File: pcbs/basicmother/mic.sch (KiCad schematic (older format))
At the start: 15 parts, among them P10 mic_conn, U7 TL082

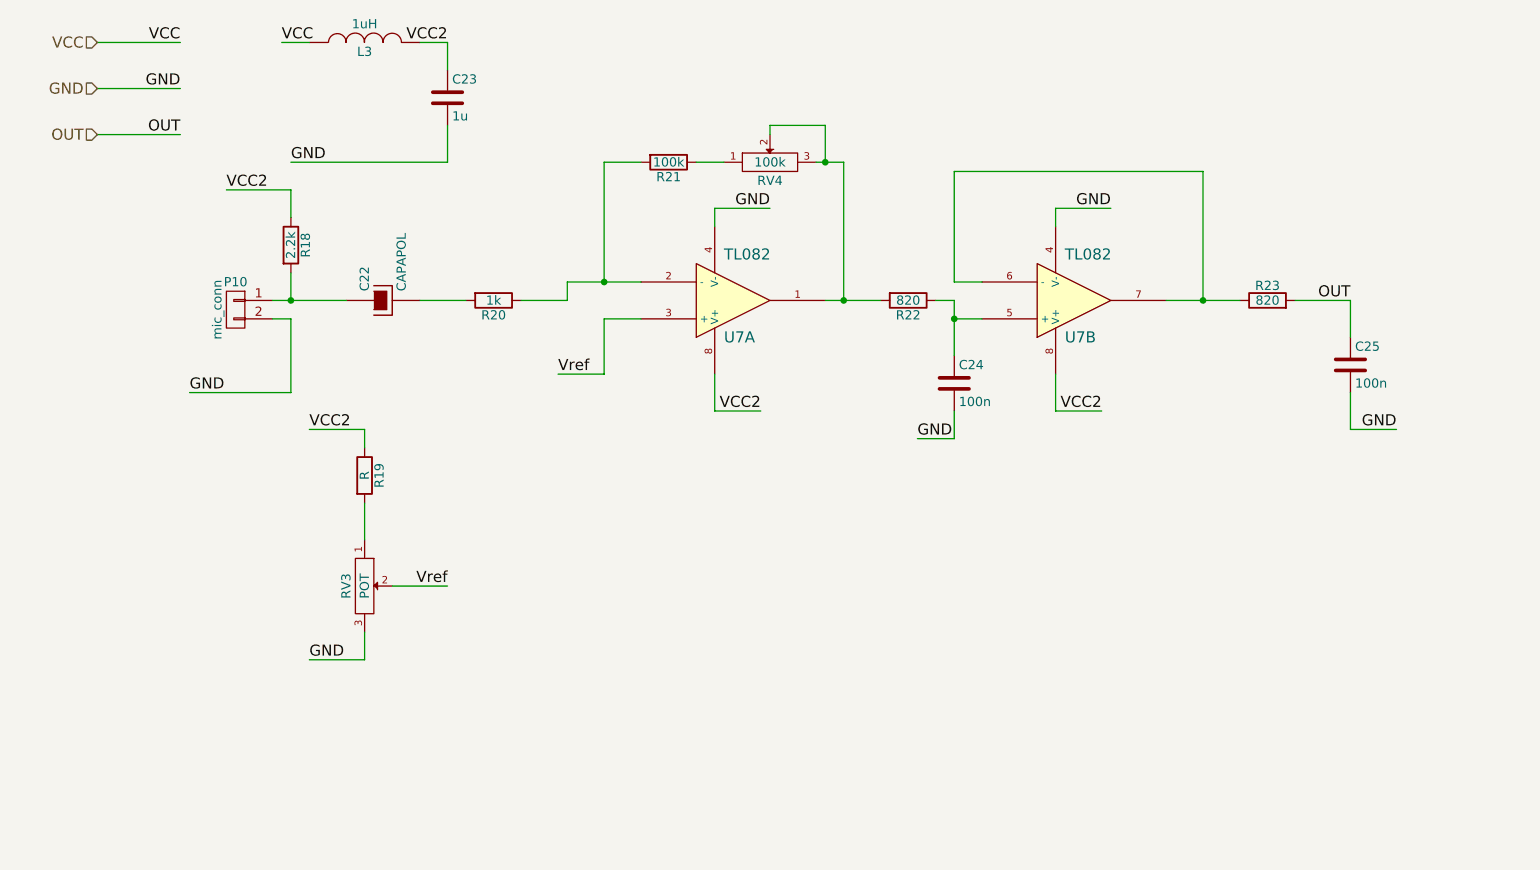
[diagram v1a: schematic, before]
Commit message: Actualizo el esquematico de la placa principal
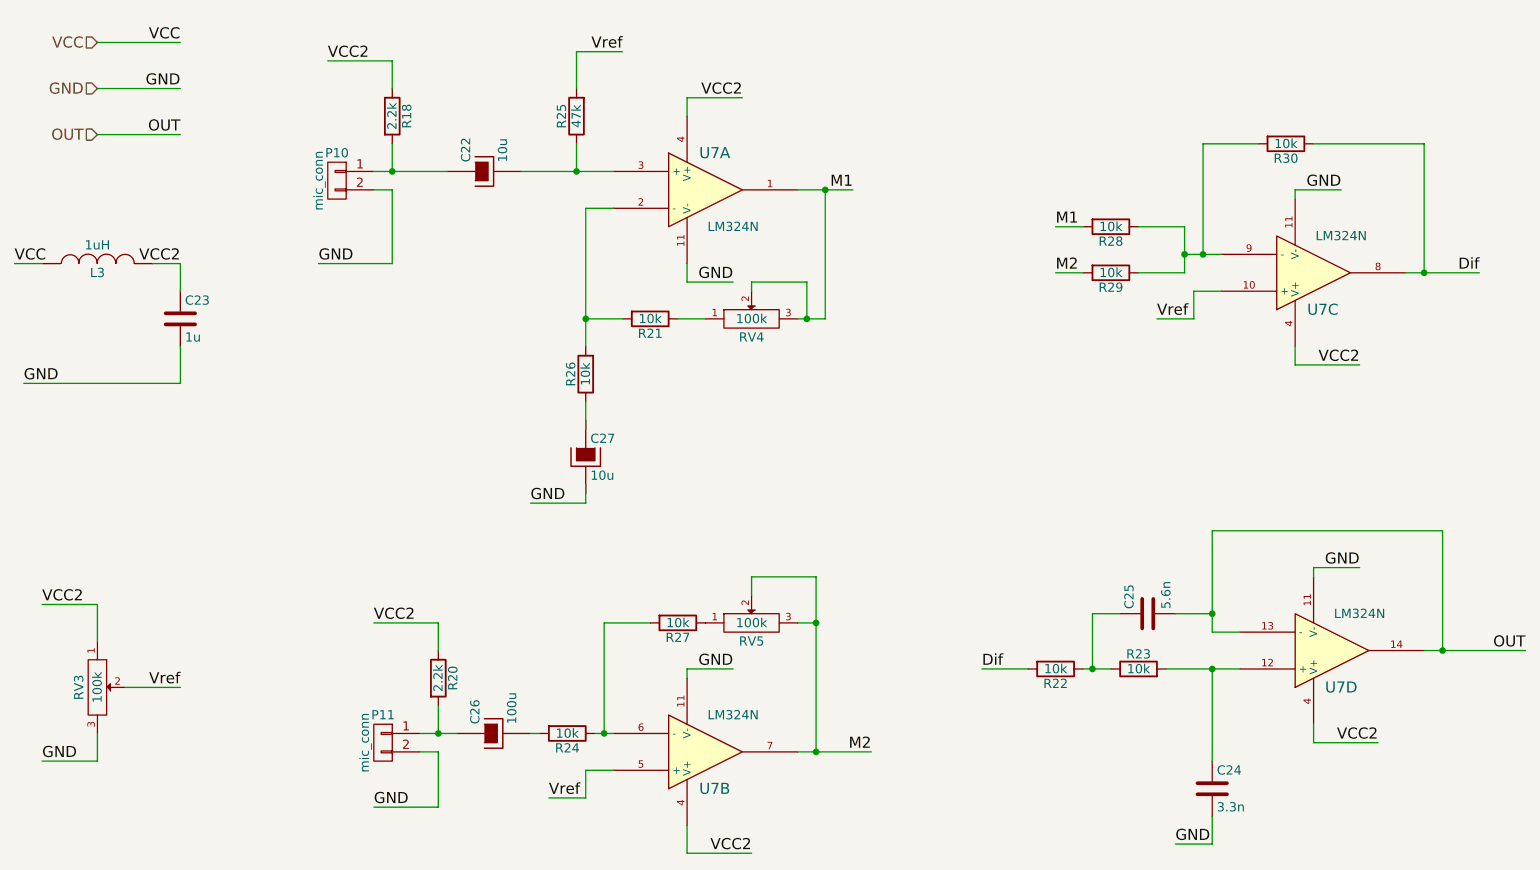
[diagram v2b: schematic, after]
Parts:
- removed R19: R, symbol R
- removed U7: TL082, symbol TL082
- added C26: 100u, symbol CAPAPOL
- added C27: 10u, symbol CP
- added P11: mic_conn, symbol CONN_01X02
- added R24, R26, R27, R28, R29, R30: 10k, symbol R
- added R25: 47k, symbol R
- added RV5: 100k, symbol POT
- added U7: LM324N, symbol LM324N
- C22: value CAPAPOL -> 10u
- C24: value 100n -> 3.3n
- C25: value 100n -> 5.6n
- R20: value 1k -> 2.2k
- R21: value 100k -> 10k
- R22, R23: value 820 -> 10k
- RV3: value POT -> 100k
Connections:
- net GND: now also P11.2 (P2), U7.11 (V-), U7.11 (V-), U7.11 (V-), U7.11 (V-); no longer C25.2
- net OUT: now also C25.2, U7.13 (-), U7.14; no longer C25.1, R23.2
- net VCC2: now also R20.1, RV3.1, U7.4 (V+), U7.4 (V+), U7.4 (V+), U7.4 (V+)
- net Vref: now also R25.2, U7.10 (+), U7.5 (+)
- net at C22.2: now also R25.1, U7.3 (+); no longer R20.2
- net M1: now reaches RV4.2, RV4.3
- net M1: now also R28.2, U7.1; no longer R22.2
- net at R21.2: now also R26.2, U7.2 (-); no longer R20.1
- net at R22.1: now also C25.1, R23.1; no longer C24.1
- new net: C24.1, R23.2, U7.12 (+)
- new net: C26.1, P11.1 (P1), R20.2
- new net: C26.2, R24.2
- new net: R28.1, R29.1, R30.2, U7.9 (-)
- new net: R24.1, R27.2, U7.6 (-)
- new net: R27.1, RV5.1
- new net Dif: R22.2, R30.1, U7.8
- new net M2: R29.2, RV5.2, RV5.3, U7.7
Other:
- moved on the sheet: C22, C23, C24, C25, L3, P10, R18, R21, R22, R23, RV3, RV4

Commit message: saque el micro para el control de los ojitos y lo pase a una placa aparte, ademas agregue un doble microfono
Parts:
- removed R30: 10k, symbol R
- added RV6: 100k, Socket_Strips:Socket_Strip_Straight_1x03, symbol POT
- C18: renamed from C23; footprint (none) -> Capacitors_ThroughHole:C_Disc_D3_P2.5
- C19: renamed from C22; footprint (none) -> Capacitors_ThroughHole:C_Disc_D3_P2.5
- C20: renamed from C26; footprint (none) -> Capacitors_ThroughHole:C_Radial_D5_L6_P2.5
- C21: renamed from C27; footprint (none) -> Capacitors_ThroughHole:C_Radial_D5_L6_P2.5
- C22: renamed from C25; footprint (none) -> Capacitors_ThroughHole:C_Disc_D3_P2.5
- C23: renamed from C24; footprint (none) -> Capacitors_ThroughHole:C_Disc_D3_P2.5
- L3, R18: footprint (none) -> Resistors_ThroughHole:Resistor_Horizontal_RM10mm
- P10: renamed from P11; footprint (none) -> Socket_Strips:Socket_Strip_Straight_1x02
- P9: renamed from P10; footprint (none) -> Socket_Strips:Socket_Strip_Straight_1x02
- R19: renamed from R20; footprint (none) -> Resistors_ThroughHole:Resistor_Horizontal_RM10mm
- R20: renamed from R24; footprint (none) -> Resistors_ThroughHole:Resistor_Horizontal_RM10mm
- R21: renamed from R25; footprint (none) -> Resistors_ThroughHole:Resistor_Horizontal_RM10mm
- R22: renamed from R26; footprint (none) -> Resistors_ThroughHole:Resistor_Horizontal_RM10mm
- R23: renamed from R21; footprint (none) -> Resistors_ThroughHole:Resistor_Horizontal_RM10mm
- R24: renamed from R27; footprint (none) -> Resistors_ThroughHole:Resistor_Horizontal_RM10mm
- R25: renamed from R22; footprint (none) -> Resistors_ThroughHole:Resistor_Horizontal_RM10mm
- R26: renamed from R28; footprint (none) -> Resistors_ThroughHole:Resistor_Horizontal_RM10mm
- R27: renamed from R29; footprint (none) -> Resistors_ThroughHole:Resistor_Horizontal_RM10mm
- R28: renamed from R23; footprint (none) -> Resistors_ThroughHole:Resistor_Horizontal_RM10mm
- RV3, RV4, RV5: footprint (none) -> Socket_Strips:Socket_Strip_Straight_1x03
- U8: renamed from U7; footprint (none) -> Sockets_DIP:DIP-14__300_ELL
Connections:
- net Dif: now also RV6.2, RV6.3
- net at R26.1, R27.1, U8.9 (-): now also RV6.1
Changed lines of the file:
@@
 $EndDescr
 $Comp
-L CONN_01X02 P10
+L CONN_01X02 P9
 U 1 1 55280813
 P 2600 1950
-F 0 "P10" H 2600 2100 50  0000 C CNN
+F 0 "P9" H 2600 2100 50  0000 C CNN
 F 1 "mic_conn" V 2700 1950 50  0000 C CNN
-F 2 "" H 2600 1950 60  0000 C CNN
+F 2 "Socket_Strips:Socket_Strip_Straight_1x02" H 2600 1950 60  0001 C CNN
 F 3 "" H 2600 1950 60  0000 C CNN
 	1    2600 1950
@@
 F 0 "R18" V 2980 1600 50  0000 C CNN
 F 1 "2.2k" V 2900 1600 50  0000 C CNN
-F 2 "" V 2830 1600 30  0000 C CNN
+F 2 "Resistors_ThroughHole:Resistor_Horizontal_RM10mm" V 2830 1600 30  0001 C CNN
 F 3 "" H 2900 1600 30  0000 C CNN
 	1    2900 1600
@@
 Connection ~ 2900 1900
 $Comp
-L CAPAPOL C22
+L CAPAPOL C19
 U 1 1 552809F6
 P 3400 1900
-F 0 "C22" H 3450 2000 50  0000 L CNN
+F 0 "C19" H 3450 2000 50  0000 L CNN
 F 1 "10u" H 3450 1800 50  0000 L CNN
-F 2 "" H 3500 1750 30  0000 C CNN
+F 2 "Capacitors_ThroughHole:C_Disc_D3_P2.5" H 3500 1750 30  0001 C CNN
 F 3 "" H 3400 1900 300 0000 C CNN
 	1    3400 1900
@@
 $EndComp
 $Comp
-L R R21
+L R R23
 U 1 1 55280CA5
 P 4300 2700
-F 0 "R21" V 4380 2700 50  0000 C CNN
+F 0 "R23" V 4380 2700 50  0000 C CNN
 F 1 "10k" V 4300 2700 50  0000 C CNN
-F 2 "" V 4230 2700 30  0000 C CNN
+F 2 "Resistors_ThroughHole:Resistor_Horizontal_RM10mm" V 4230 2700 30  0001 C CNN
 F 3 "" H 4300 2700 30  0000 C CNN
 	1    4300 2700
@@
 	4150 2700 3950 2700
 $Comp
-L R R22
+L R R25
 U 1 1 55280E9E
 P 6500 4600
-F 0 "R22" V 6580 4600 50  0000 C CNN
+F 0 "R25" V 6580 4600 50  0000 C CNN
 F 1 "10k" V 6500 4600 50  0000 C CNN
-F 2 "" V 6430 4600 30  0000 C CNN
+F 2 "Resistors_ThroughHole:Resistor_Horizontal_RM10mm" V 6430 4600 30  0001 C CNN
 F 3 "" H 6500 4600 30  0000 C CNN
 	1    6500 4600
@@
 F 0 "RV3" H 1300 4600 50  0000 C CNN
 F 1 "100k" H 1300 4700 50  0000 C CNN
-F 2 "" H 1300 4700 60  0000 C CNN
+F 2 "Socket_Strips:Socket_Strip_Straight_1x03" H 1300 4700 60  0001 C CNN
 F 3 "" H 1300 4700 60  0000 C CNN
 	1    1300 4700
@@
 Vref
 $Comp
-L R R23
+L R R28
 U 1 1 552815BA
 P 6950 4600
-F 0 "R23" V 7030 4600 50  0000 C CNN
+F 0 "R28" V 7030 4600 50  0000 C CNN
 F 1 "10k" V 6950 4600 50  0000 C CNN
-F 2 "" V 6880 4600 30  0000 C CNN
+F 2 "Resistors_ThroughHole:Resistor_Horizontal_RM10mm" V 6880 4600 30  0001 C CNN
 F 3 "" H 6950 4600 30  0000 C CNN
 	1    6950 4600
@@
 $EndComp
 $Comp
-L C C25
+L C C22
 U 1 1 55281618
 P 7000 4300
-F 0 "C25" H 7025 4400 50  0000 L CNN
+F 0 "C22" H 7025 4400 50  0000 L CNN
 F 1 "5.6n" H 7025 4200 50  0000 L CNN
-F 2 "" H 7038 4150 30  0000 C CNN
+F 2 "Capacitors_ThroughHole:C_Disc_D3_P2.5" H 7038 4150 30  0001 C CNN
 F 3 "" H 7000 4300 60  0000 C CNN
 	1    7000 4300
@@
 $EndComp
 $Comp
-L C C24
+L C C23
 U 1 1 55287955
 P 7350 5250
-F 0 "C24" H 7375 5350 50  0000 L CNN
+F 0 "C23" H 7375 5350 50  0000 L CNN
 F 1 "3.3n" H 7375 5150 50  0000 L CNN
-F 2 "" H 7388 5100 30  0000 C CNN
+F 2 "Capacitors_ThroughHole:C_Disc_D3_P2.5" H 7388 5100 30  0001 C CNN
 F 3 "" H 7350 5250 60  0000 C CNN
 	1    7350 5250
@@
 F 0 "RV4" H 4850 2600 50  0000 C CNN
 F 1 "100k" H 4850 2700 50  0000 C CNN
-F 2 "" H 4850 2700 60  0000 C CNN
+F 2 "Socket_Strips:Socket_Strip_Straight_1x03" H 4850 2700 60  0001 C CNN
 F 3 "" H 4850 2700 60  0000 C CNN
 	1    4850 2700
@@
 F 0 "L3" V 1250 2400 50  0000 C CNN
 F 1 "1uH" V 1400 2400 50  0000 C CNN
-F 2 "" H 1300 2400 60  0000 C CNN
+F 2 "Resistors_ThroughHole:Resistor_Horizontal_RM10mm" H 1300 2400 60  0001 C CNN
 F 3 "" H 1300 2400 60  0000 C CNN
 	1    1300 2400
@@
 $EndComp
 $Comp
-L C C23
+L C C18
 U 1 1 55288DAC
 P 1750 2700
-F 0 "C23" H 1775 2800 50  0000 L CNN
+F 0 "C18" H 1775 2800 50  0000 L CNN
 F 1 "1u" H 1775 2600 50  0000 L CNN
-F 2 "" H 1788 2550 30  0000 C CNN
+F 2 "Capacitors_ThroughHole:C_Disc_D3_P2.5" H 1788 2550 30  0001 C CNN
 F 3 "" H 1750 2700 60  0000 C CNN
 	1    1750 2700
@@
 OUT
 $Comp
-L CONN_01X02 P11
+L CONN_01X02 P10
 U 1 1 5531C027
 P 2850 5000
-F 0 "P11" H 2850 5150 50  0000 C CNN
+F 0 "P10" H 2850 5150 50  0000 C CNN
 F 1 "mic_conn" V 2950 5000 50  0000 C CNN
-F 2 "" H 2850 5000 60  0000 C CNN
+F 2 "Socket_Strips:Socket_Strip_Straight_1x02" H 2850 5000 60  0001 C CNN
 F 3 "" H 2850 5000 60  0000 C CNN
 	1    2850 5000
@@
 $EndComp
 $Comp
-L R R20
+L R R19
 U 1 1 5531C02D
 P 3150 4650
-F 0 "R20" V 3230 4650 50  0000 C CNN
+F 0 "R19" V 3230 4650 50  0000 C CNN
 F 1 "2.2k" V 3150 4650 50  0000 C CNN
-F 2 "" V 3080 4650 30  0000 C CNN
+F 2 "Resistors_ThroughHole:Resistor_Horizontal_RM10mm" V 3080 4650 30  0001 C CNN
 F 3 "" H 3150 4650 30  0000 C CNN
 	1    3150 4650
@@
 Connection ~ 3150 4950
 $Comp
-L CAPAPOL C26
+L CAPAPOL C20
 U 1 1 5531C03D
 P 3450 4950
-F 0 "C26" H 3500 5050 50  0000 L CNN
+F 0 "C20" H 3500 5050 50  0000 L CNN
 F 1 "100u" H 3500 4850 50  0000 L CNN
-F 2 "" H 3550 4800 30  0000 C CNN
+F 2 "Capacitors_ThroughHole:C_Radial_D5_L6_P2.5" H 3550 4800 30  0001 C CNN
 F 3 "" H 3450 4950 300 0000 C CNN
 	1    3450 4950
@@
 $EndComp
 $Comp
-L R R25
+L R R21
 U 1 1 5531C7F1
 P 3900 1600
-F 0 "R25" V 3980 1600 50  0000 C CNN
+F 0 "R21" V 3980 1600 50  0000 C CNN
 F 1 "47k" V 3900 1600 50  0000 C CNN
-F 2 "" V 3830 1600 30  0000 C CNN
+F 2 "Resistors_ThroughHole:Resistor_Horizontal_RM10mm" V 3830 1600 30  0001 C CNN
 F 3 "" H 3900 1600 30  0000 C CNN
 	1    3900 1600
@@
 Connection ~ 3950 2700
 $Comp
-L R R26
+L R R22
 U 1 1 5531D46C
 P 3950 3000
-F 0 "R26" V 4030 3000 50  0000 C CNN
+F 0 "R22" V 4030 3000 50  0000 C CNN
 F 1 "10k" V 3950 3000 50  0000 C CNN
-F 2 "" V 3880 3000 30  0000 C CNN
+F 2 "Resistors_ThroughHole:Resistor_Horizontal_RM10mm" V 3880 3000 30  0001 C CNN
 F 3 "" H 3950 3000 30  0000 C CNN
 	1    3950 3000
@@
 $EndComp
 $Comp
-L CP C27
+L CP C21
 U 1 1 5531D5DC
 P 3950 3450
-F 0 "C27" H 3975 3550 50  0000 L CNN
+F 0 "C21" H 3975 3550 50  0000 L CNN
 F 1 "10u" H 3975 3350 50  0000 L CNN
-F 2 "" H 3988 3300 30  0000 C CNN
+F 2 "Capacitors_ThroughHole:C_Radial_D5_L6_P2.5" H 3988 3300 30  0001 C CNN
 F 3 "" H 3950 3450 60  0000 C CNN
 	1    3950 3450
@@
 	3950 3700 3950 3600
 $Comp
-L R R28
+L R R26
 U 1 1 5531DA83
 P 6800 2200
-F 0 "R28" V 6880 2200 50  0000 C CNN
+F 0 "R26" V 6880 2200 50  0000 C CNN
 F 1 "10k" V 6800 2200 50  0000 C CNN
-F 2 "" V 6730 2200 30  0000 C CNN
+F 2 "Resistors_ThroughHole:Resistor_Horizontal_RM10mm" V 6730 2200 30  0001 C CNN
 F 3 "" H 6800 2200 30  0000 C CNN
 	1    6800 2200
@@
 GND
 $Comp
-L LM324N U7
+L LM324N U8
 U 1 1 5531E6C6
 P 4600 2000
-F 0 "U7" H 4650 2200 60  0000 C CNN
+F 0 "U8" H 4650 2200 60  0000 C CNN
 F 1 "LM324N" H 4750 1800 50  0000 C CNN
-F 2 "" H 4600 2000 60  0000 C CNN
+F 2 "Sockets_DIP:DIP-14__300_ELL" H 4600 2000 60  0001 C CNN
 F 3 "" H 4600 2000 60  0000 C CNN
 	1    4600 2000
@@
 $EndComp
 $Comp
-L LM324N U7
+L LM324N U8
 U 2 1 5531E7AD
 P 4600 5050
-F 0 "U7" H 4650 5250 60  0000 C CNN
+F 0 "U8" H 4650 5250 60  0000 C CNN
 F 1 "LM324N" H 4750 4850 50  0000 C CNN
-F 2 "" H 4600 5050 60  0000 C CNN
+F 2 "Sockets_DIP:DIP-14__300_ELL" H 4600 5050 60  0001 C CNN
 F 3 "" H 4600 5050 60  0000 C CNN
 	2    4600 5050
@@
 $EndComp
 $Comp
-L R R24
+L R R20
 U 1 1 5531EE20
 P 3850 4950
-F 0 "R24" V 3930 4950 50  0000 C CNN
+F 0 "R20" V 3930 4950 50  0000 C CNN
 F 1 "10k" V 3850 4950 50  0000 C CNN
-F 2 "" V 3780 4950 30  0000 C CNN
+F 2 "Resistors_ThroughHole:Resistor_Horizontal_RM10mm" V 3780 4950 30  0001 C CNN
 F 3 "" H 3850 4950 30  0000 C CNN
 	1    3850 4950
@@
 Connection ~ 4050 4950
 $Comp
-L R R27
+L R R24
 U 1 1 5531F00F
 P 4450 4350
-F 0 "R27" V 4530 4350 50  0000 C CNN
+F 0 "R24" V 4530 4350 50  0000 C CNN
 F 1 "10k" V 4450 4350 50  0000 C CNN
-F 2 "" V 4380 4350 30  0000 C CNN
+F 2 "Resistors_ThroughHole:Resistor_Horizontal_RM10mm" V 4380 4350 30  0001 C CNN
 F 3 "" H 4450 4350 30  0000 C CNN
 	1    4450 4350
@@
 F 0 "RV5" H 4850 4250 50  0000 C CNN
 F 1 "100k" H 4850 4350 50  0000 C CNN
-F 2 "" H 4850 4350 60  0000 C CNN
+F 2 "Socket_Strips:Socket_Strip_Straight_1x03" H 4850 4350 60  0001 C CNN
 F 3 "" H 4850 4350 60  0000 C CNN
 	1    4850 4350
@@
 Connection ~ 5200 5050
 $Comp
-L R R29
+L R R27
 U 1 1 5531F338
 P 6800 2450
-F 0 "R29" V 6880 2450 50  0000 C CNN
+F 0 "R27" V 6880 2450 50  0000 C CNN
 F 1 "10k" V 6800 2450 50  0000 C CNN
-F 2 "" V 6730 2450 30  0000 C CNN
+F 2 "Resistors_ThroughHole:Resistor_Horizontal_RM10mm" V 6730 2450 30  0001 C CNN
 F 3 "" H 6800 2450 30  0000 C CNN
 	1    6800 2450
@@
 	7200 2450 6950 2450
 $Comp
-L LM324N U7
+L LM324N U8
 U 3 1 5531FD04
 P 7900 2450
-F 0 "U7" H 7950 2650 60  0000 C CNN
+F 0 "U8" H 7950 2650 60  0000 C CNN
 F 1 "LM324N" H 8050 2250 50  0000 C CNN
-F 2 "" H 7900 2450 60  0000 C CNN
+F 2 "Sockets_DIP:DIP-14__300_ELL" H 7900 2450 60  0001 C CNN
 F 3 "" H 7900 2450 60  0000 C CNN
 	3    7900 2450
@@
 Wire Wire Line
 	7300 2350 7300 1750
-Wire Wire Line
-	7300 1750 7600 1750
 Connection ~ 7300 2350
 Wire Wire Line
@@
 	8400 2450 8800 2450
 $Comp
-L R R30
-U 1 1 5532123E
-P 7750 1750
-F 0 "R30" V 7830 1750 50  0000 C CNN
-F 1 "10k" V 7750 1750 50  0000 C CNN
-F 2 "" V 7680 1750 30  0000 C CNN
-F 3 "" H 7750 1750 30  0000 C CNN
-	1    7750 1750
-	0    1    1    0
-$EndComp
-Wire Wire Line
-	7900 1750 8500 1750
-$Comp
-L LM324N U7
+L LM324N U8
 U 4 1 553213C0
 P 8000 4500
-F 0 "U7" H 8050 4700 60  0000 C CNN
+F 0 "U8" H 8050 4700 60  0000 C CNN
 F 1 "LM324N" H 8150 4300 50  0000 C CNN
-F 2 "" H 8000 4500 60  0000 C CNN
+F 2 "Sockets_DIP:DIP-14__300_ELL" H 8000 4500 60  0001 C CNN
 F 3 "" H 8000 4500 60  0000 C CNN
 	4    8000 4500
@@
 Text Label 9050 4500 2    60   ~ 0
 OUT
+$Comp
+L POT RV6
+U 1 1 5532F8CB
+P 7850 1750
+F 0 "RV6" H 7850 1650 50  0000 C CNN
+F 1 "100k" H 7850 1750 50  0000 C CNN
+F 2 "Socket_Strips:Socket_Strip_Straight_1x03" H 7850 1750 60  0001 C CNN
+F 3 "" H 7850 1750 60  0000 C CNN
+	1    7850 1750
+	1    0    0    -1
+$EndComp
+Wire Wire Line
+	8100 1750 8500 1750
+Wire Wire Line
+	7300 1750 7600 1750
+Wire Wire Line
+	7850 1600 7850 1550
+Wire Wire Line
+	8150 1550 8150 1750
+Connection ~ 8150 1750
+Wire Wire Line
+	7850 1550 8150 1550
 $EndSCHEMATC

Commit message: primera version del pcb de la placa principal, falta verificar footprints
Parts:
- C19: footprint Capacitors_ThroughHole:C_Disc_D3_P2.5 -> Capacitors_ThroughHole:C_Radial_D5_L6_P2.5
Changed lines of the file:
@@
 F 0 "C19" H 3450 2000 50  0000 L CNN
 F 1 "10u" H 3450 1800 50  0000 L CNN
-F 2 "Capacitors_ThroughHole:C_Disc_D3_P2.5" H 3500 1750 30  0001 C CNN
+F 2 "Capacitors_ThroughHole:C_Radial_D5_L6_P2.5" H 3500 1750 30  0001 C CNN
 F 3 "" H 3400 1900 300 0000 C CNN
 	1    3400 1900

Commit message: actualizo las 3 placas, revisar y mandar a fabricar
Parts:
- C18: footprint Capacitors_ThroughHole:C_Disc_D3_P2.5 -> Capacitors_ThroughHole:C_Rect_L18_W5_P15
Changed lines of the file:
@@
 F 0 "C18" H 1775 2800 50  0000 L CNN
 F 1 "1u" H 1775 2600 50  0000 L CNN
-F 2 "Capacitors_ThroughHole:C_Disc_D3_P2.5" H 1788 2550 30  0001 C CNN
+F 2 "Capacitors_ThroughHole:C_Rect_L18_W5_P15" H 1788 2550 30  0001 C CNN
 F 3 "" H 1750 2700 60  0000 C CNN
 	1    1750 2700
